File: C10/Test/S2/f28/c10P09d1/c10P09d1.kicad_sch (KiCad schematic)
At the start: 3 parts

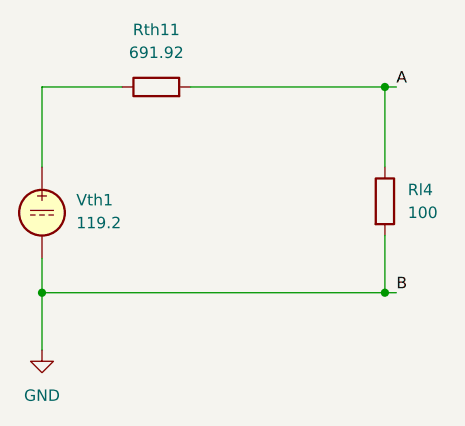
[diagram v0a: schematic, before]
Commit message: corrected from misprinting Fig 10-28
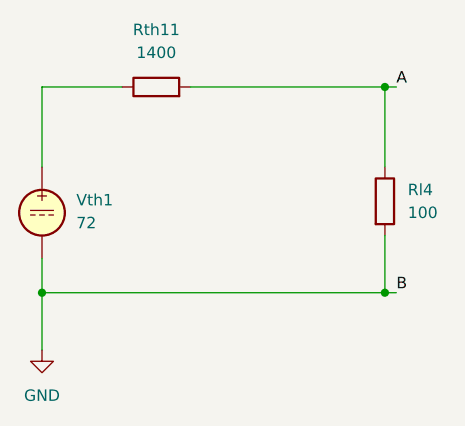
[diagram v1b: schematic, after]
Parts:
- Rth11: value 691.92 -> 1400
- Vth1: value 119.2 -> 72
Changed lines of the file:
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@@
 			)
 		)
-		(property "Value" "119.2"
+		(property "Value" "72"
 			(at 139.7 84.9601 0)
 			(show_name no)
@@
 			)
 		)
-		(property "Value" "691.92"
+		(property "Value" "1400"
 			(at 148.59 66.04 90)
 			(show_name no)
